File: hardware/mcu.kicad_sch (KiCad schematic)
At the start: 20 parts, among them J301 TagConnect, J302 USER CONN., U301 STM32G431, U302 SN65HVD230, Y301 12MHz

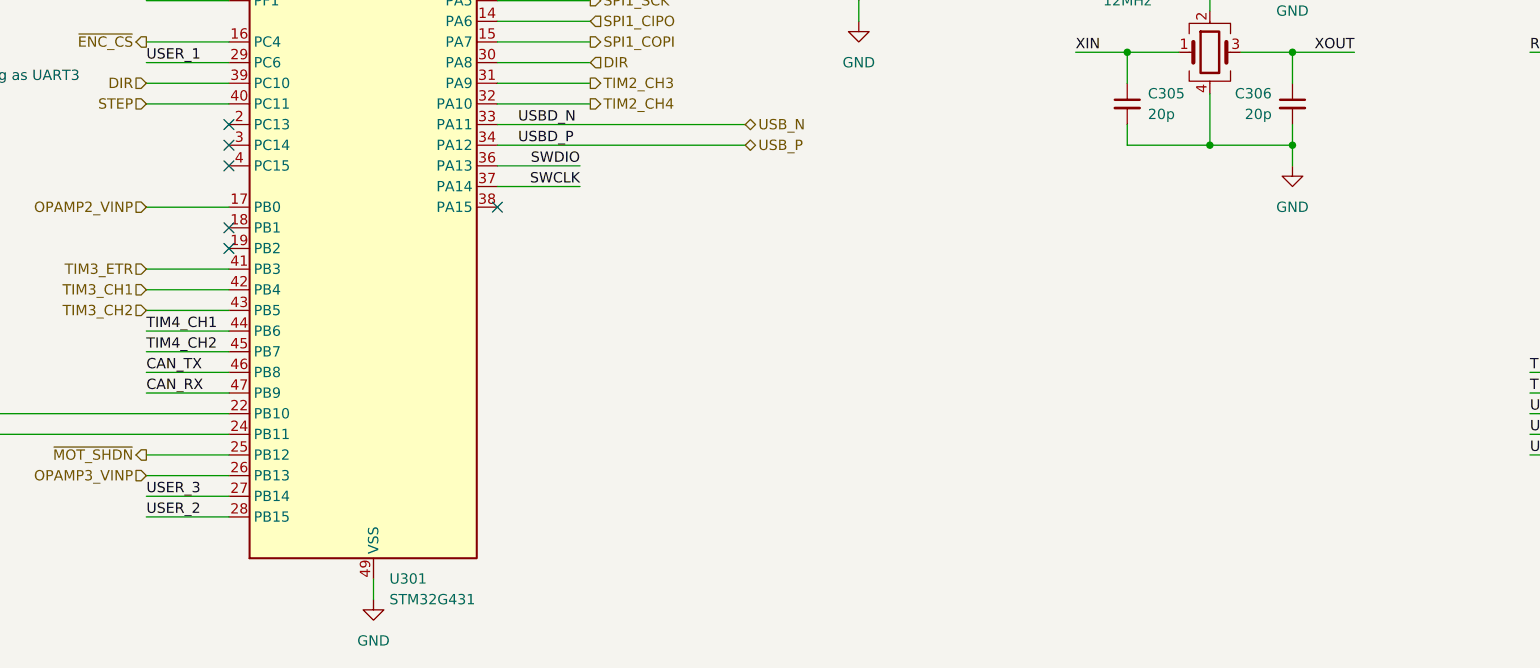
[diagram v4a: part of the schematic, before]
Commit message: add user button
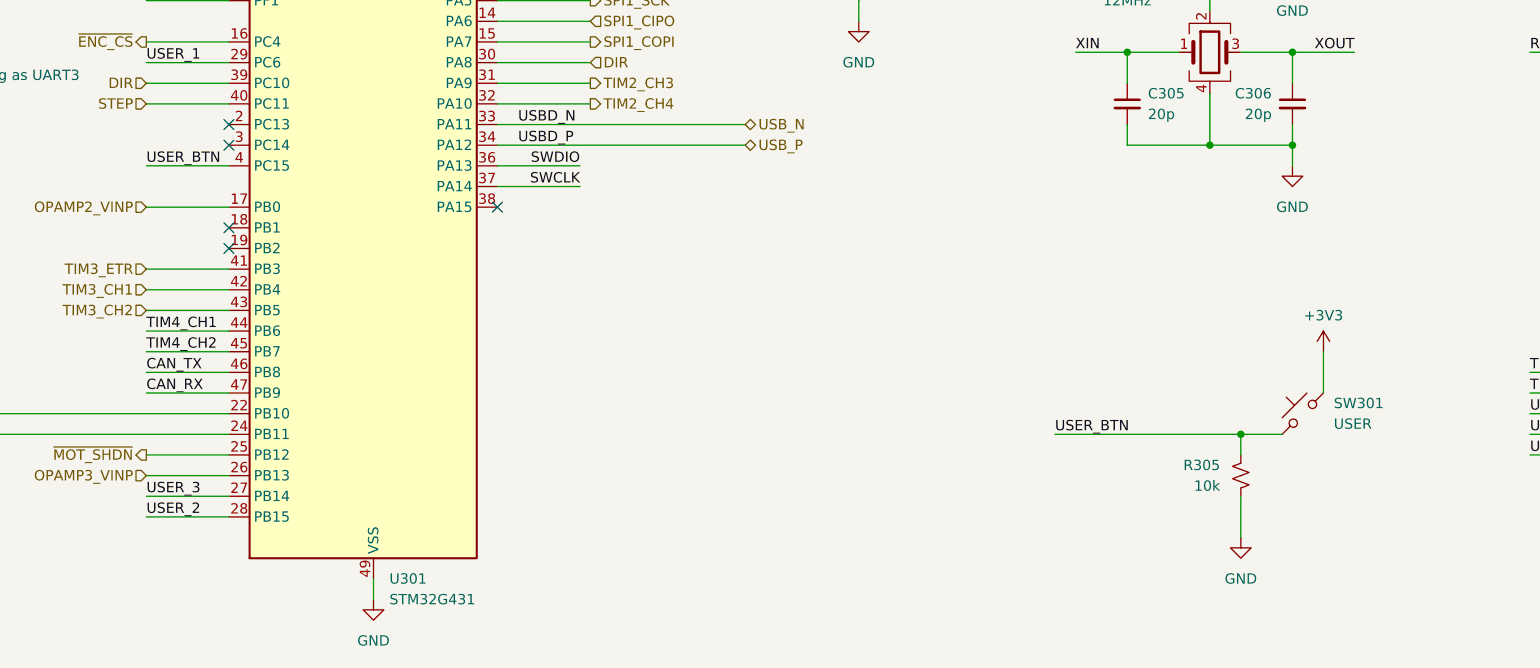
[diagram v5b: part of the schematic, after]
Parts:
- added R305: 10k, Resistor_SMD:R_0402_1005Metric, symbol Device:R_Small_US
- added SW301: USER, Button_Switch_SMD:SW_SPST_B3U-3000P, symbol Switch:SW_Push_45deg
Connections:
- net +3V3: now also SW301.2
- net GND: now also R305.2
- net USER_BTN: now reaches U301.4 (PC15)
- net USER_BTN: now also R305.1, SW301.1
- no-connect marks 10 -> 9
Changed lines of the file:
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@@
   (junction (at 186.69 90.17) (diameter 0) (color 0 0 0 0)
+  )
+  (junction (at 200.66 137.16) (diameter 0) (color 0 0 0 0)
   )
   (junction (at 123.19 52.07) (diameter 0) (color 0 0 0 0)
@@
   (no_connect (at 88.9 66.04))
   (no_connect (at 76.2 99.06))
-  (no_connect (at 76.2 104.14))
   (no_connect (at 76.2 111.76))
   (no_connect (at 76.2 114.3))
@@
     (stroke (width 0) (type default))
   )
+  (wire (pts (xy 200.66 137.16) (xy 205.74 137.16))
+    (stroke (width 0) (type default))
+  )
   (wire (pts (xy 232.41 48.26) (xy 243.84 48.26))
     (stroke (width 0) (type default))
@@
     (stroke (width 0) (type default))
   )
+  (wire (pts (xy 177.8 137.16) (xy 200.66 137.16))
+    (stroke (width 0) (type default))
+  )
   (wire (pts (xy 153.67 83.82) (xy 153.67 86.36))
     (stroke (width 0) (type default))
@@
     (stroke (width 0) (type default))
   )
+  (wire (pts (xy 210.82 127) (xy 210.82 132.08))
+    (stroke (width 0) (type default))
+  )
   (wire (pts (xy 123.19 58.42) (xy 123.19 59.69))
     (stroke (width 0) (type default))
@@
     (stroke (width 0) (type default))
   )
+  (wire (pts (xy 200.66 139.7) (xy 200.66 137.16))
+    (stroke (width 0) (type default))
+  )
   (wire (pts (xy 66.04 144.78) (xy 76.2 144.78))
     (stroke (width 0) (type default))
@@
     (stroke (width 0) (type default))
   )
+  (wire (pts (xy 66.04 104.14) (xy 76.2 104.14))
+    (stroke (width 0) (type default))
+  )
   (wire (pts (xy 133.35 52.07) (xy 133.35 53.34))
     (stroke (width 0) (type default))
@@
   )
   (wire (pts (xy 54.61 78.74) (xy 44.45 78.74))
+    (stroke (width 0) (type default))
+  )
+  (wire (pts (xy 200.66 144.78) (xy 200.66 149.86))
     (stroke (width 0) (type default))
   )
@@
     (effects (font (size 1.27 1.27)) (justify left bottom))
   )
+  (label "USER_BTN" (at 66.04 104.14 0) (fields_autoplaced)
+    (effects (font (size 1.27 1.27)) (justify left bottom))
+  )
   (label "USBD_N" (at 111.76 99.06 0) (fields_autoplaced)
     (effects (font (size 1.27 1.27)) (justify left bottom))
@@
   )
   (label "TIM4_CH1" (at 66.04 124.46 0) (fields_autoplaced)
+    (effects (font (size 1.27 1.27)) (justify left bottom))
+  )
+  (label "USER_BTN" (at 177.8 137.16 0) (fields_autoplaced)
     (effects (font (size 1.27 1.27)) (justify left bottom))
   )
@@
     )
   )
+  (symbol (lib_id "power:GND") (at 200.66 149.86 0) (unit 1)
+    (in_bom yes) (on_board yes) (dnp no) (fields_autoplaced)
+    (property "Reference" "#PWR0318" (at 200.66 156.21 0)
+      (effects (font (size 1.27 1.27)) hide)
+    )
+    (property "Value" "GND" (at 200.66 154.94 0)
+      (effects (font (size 1.27 1.27)))
+    )
+    (property "Footprint" "" (at 200.66 149.86 0)
+      (effects (font (size 1.27 1.27)) hide)
+    )
+    (property "Datasheet" "" (at 200.66 149.86 0)
+      (effects (font (size 1.27 1.27)) hide)
+    )
+    (pin "1")
+    (instances
+      (project "lemon-pepper"
+        (path "/0306e2fa-4433-4288-91d9-65a3484207ad/7f2d245a-6dca-4eb9-9839-7fdf255edd98"
+          (reference "#PWR0318") (unit 1)
+        )
+      )
+      (project "stm32g431-mt6701-stspin233"
+        (path "/bcb2c98d-7159-437a-9ffb-b81c5fcc4307"
+          (reference "#PWR0106") (unit 1)
+        )
+        (path "/bcb2c98d-7159-437a-9ffb-b81c5fcc4307/ed84ebbf-b2e5-4959-b495-bf58cd9b4c8c"
+          (reference "#PWR0204") (unit 1)
+        )
+      )
+    )
+  )
+  (symbol (lib_id "power:+3V3") (at 210.82 127 0) (unit 1)
+    (in_bom yes) (on_board yes) (dnp no) (fields_autoplaced)
+    (property "Reference" "#PWR0317" (at 210.82 130.81 0)
+      (effects (font (size 1.27 1.27)) hide)
+    )
+    (property "Value" "+3V3" (at 210.82 122.555 0)
+      (effects (font (size 1.27 1.27)))
+    )
+    (property "Footprint" "" (at 210.82 127 0)
+      (effects (font (size 1.27 1.27)) hide)
+    )
+    (property "Datasheet" "" (at 210.82 127 0)
+      (effects (font (size 1.27 1.27)) hide)
+    )
+    (pin "1")
+    (instances
+      (project "lemon-pepper"
+        (path "/0306e2fa-4433-4288-91d9-65a3484207ad/7f2d245a-6dca-4eb9-9839-7fdf255edd98"
+          (reference "#PWR0317") (unit 1)
+        )
+      )
+      (project "stm32g431-mt6701-stspin233"
+        (path "/bcb2c98d-7159-437a-9ffb-b81c5fcc4307"
+          (reference "#PWR0123") (unit 1)
+        )
+        (path "/bcb2c98d-7159-437a-9ffb-b81c5fcc4307/ed84ebbf-b2e5-4959-b495-bf58cd9b4c8c"
+          (reference "#PWR0210") (unit 1)
+        )
+      )
+    )
+  )
   (symbol (lib_id "Device:LED") (at 38.1 151.13 90) (unit 1)
     (in_bom yes) (on_board yes) (dnp no) (fields_autoplaced)
@@
         (path "/bcb2c98d-7159-437a-9ffb-b81c5fcc4307/ed84ebbf-b2e5-4959-b495-bf58cd9b4c8c"
           (reference "#PWR0210") (unit 1)
+        )
+      )
+    )
+  )
+  (symbol (lib_id "Switch:SW_Push_45deg") (at 208.28 134.62 90) (unit 1)
+    (in_bom yes) (on_board yes) (dnp no) (fields_autoplaced)
+    (property "Reference" "SW301" (at 212.09 133.35 90)
+      (effects (font (size 1.27 1.27)) (justify right))
+    )
+    (property "Value" "USER" (at 212.09 135.89 90)
+      (effects (font (size 1.27 1.27)) (justify right))
+    )
+    (property "Footprint" "Button_Switch_SMD:SW_SPST_B3U-3000P" (at 208.28 134.62 0)
+      (effects (font (size 1.27 1.27)) hide)
+    )
+    (property "Datasheet" "~" (at 208.28 134.62 0)
+      (effects (font (size 1.27 1.27)) hide)
+    )
+    (pin "1")
+    (pin "2")
+    (instances
+      (project "lemon-pepper"
+        (path "/0306e2fa-4433-4288-91d9-65a3484207ad/7f2d245a-6dca-4eb9-9839-7fdf255edd98"
+          (reference "SW301") (unit 1)
         )
       )
@@
         )
       )
+    )
+  )
+  (symbol (lib_id "Device:R_Small_US") (at 200.66 142.24 0) (mirror y) (unit 1)
+    (in_bom yes) (on_board yes) (dnp no)
+    (property "Reference" "R305" (at 198.12 140.97 0)
+      (effects (font (size 1.27 1.27)) (justify left))
+    )
+    (property "Value" "10k" (at 198.12 143.51 0)
+      (effects (font (size 1.27 1.27)) (justify left))
+    )
+    (property "Footprint" "Resistor_SMD:R_0402_1005Metric" (at 200.66 142.24 0)
+      (effects (font (size 1.27 1.27)) hide)
+    )
+    (property "Datasheet" "~" (at 200.66 142.24 0)
+      (effects (font (size 1.27 1.27)) hide)
+    )
+    (property "LCSC Part" "C25744" (at 200.66 142.24 0)
+      (effects (font (size 1.27 1.27)) hide)
+    )
+    (pin "1")
+    (pin "2")
+    (instances
+      (project "lemon-pepper"
+        (path "/0306e2fa-4433-4288-91d9-65a3484207ad/7f2d245a-6dca-4eb9-9839-7fdf255edd98"
+          (reference "R305") (unit 1)
+        )
+      )
+      (project "stm32g431-mt6701-stspin233"
+        (path "/bcb2c98d-7159-437a-9ffb-b81c5fcc4307"
+          (reference "R?") (unit 1)
+        )
+        (path "/bcb2c98d-7159-437a-9ffb-b81c5fcc4307/ed84ebbf-b2e5-4959-b495-bf58cd9b4c8c"
+          (reference "R203") (unit 1)
+        )
+      )

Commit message: finalize v3 files
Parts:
- SW301: LCSC Part (none) -> C963349
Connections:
- net LED_GOOD: now reaches R301.1, U301.22 (PB10)
- net LED_FAULT: now reaches R302.1, U301.24 (PB11)
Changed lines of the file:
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@@
+    (effects (font (size 1.27 1.27)) (justify left bottom))
+  )
+  (label "LED_GOOD" (at 66.04 134.62 0) (fields_autoplaced)
     (effects (font (size 1.27 1.27)) (justify left bottom))
   )
@@
     (effects (font (size 1.27 1.27)) (justify left bottom))
   )
+  (label "LED_FAULT" (at 66.04 137.16 0) (fields_autoplaced)
+    (effects (font (size 1.27 1.27)) (justify left bottom))
+  )
   (label "USER_1" (at 66.04 91.44 0) (fields_autoplaced)
     (effects (font (size 1.27 1.27)) (justify left bottom))
@@
       (effects (font (size 1.27 1.27)) hide)
     )
+    (property "LCSC Part" "C963349" (at 208.28 134.62 0)
+      (effects (font (size 1.27 1.27)) hide)
+    )

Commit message: rev3 documentation
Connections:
- net OPAMP2_VINP: no longer names the net of U301.17 (PB0)
- no-connect marks 9 -> 10
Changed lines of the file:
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@@
   (no_connect (at 109.22 76.2))
   (no_connect (at 76.2 101.6))
+  (no_connect (at 76.2 109.22))
   (no_connect (at 189.23 48.26))
   (no_connect (at 88.9 66.04))
@@
     (stroke (width 0) (type default))
   )
-  (wire (pts (xy 66.04 109.22) (xy 76.2 109.22))
-    (stroke (width 0) (type default))
-  )
   (wire (pts (xy 54.61 78.74) (xy 44.45 78.74))
     (stroke (width 0) (type default))
@@
     (effects (font (size 1.27 1.27)) (justify right))
   )
-  (hierarchical_label "OPAMP2_VINP" (shape input) (at 66.04 109.22 180) (fields_autoplaced)
-    (effects (font (size 1.27 1.27)) (justify right))
-  )

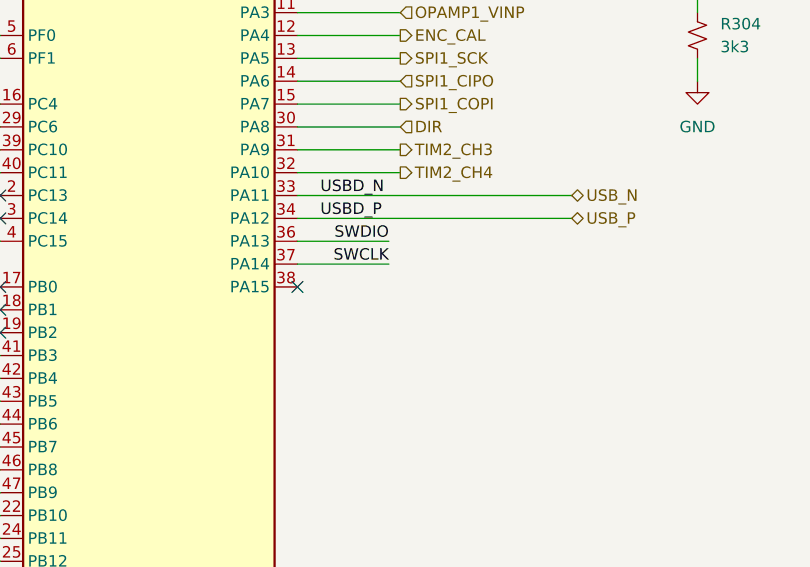
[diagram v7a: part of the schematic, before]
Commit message: change inductor footprint, add I2C1 SCL on user 3
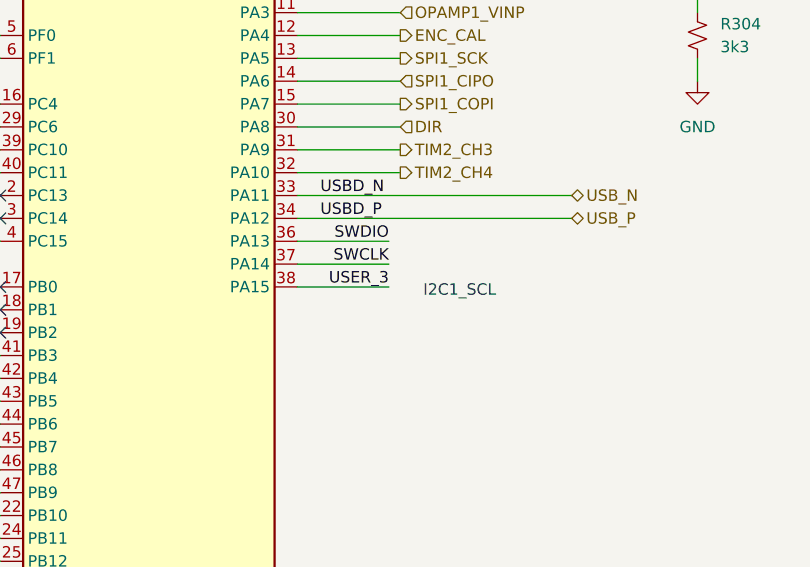
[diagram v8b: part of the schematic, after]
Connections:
- net USER_3: now also U301.38 (PA15)
- no-connect marks 10 -> 9
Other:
- note added: "I2C1_SCL"
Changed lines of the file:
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@@
   )
   (no_connect (at 243.84 50.8))
-  (no_connect (at 109.22 109.22))
   (no_connect (at 109.22 76.2))
   (no_connect (at 76.2 101.6))
@@
     (stroke (width 0) (type default))
   )
+  (wire (pts (xy 109.22 109.22) (xy 119.38 109.22))
+    (stroke (width 0) (type default))
+  )
   (wire (pts (xy 143.51 52.07) (xy 143.51 53.34))
     (stroke (width 0) (type default))
@@
   (wire (pts (xy 199.39 57.15) (xy 199.39 58.42))
     (stroke (width 0) (type default))
+  )
+  (text "I2C1_SCL" (at 123.19 110.49 0)
+    (effects (font (size 1.27 1.27)) (justify left bottom))
   )
   (text "really acting as UART3" (at 38.1 93.98 0)
@@
     (effects (font (size 1.27 1.27)) (justify left bottom))
   )
+  (label "USER_3" (at 119.38 109.22 180) (fields_autoplaced)
+    (effects (font (size 1.27 1.27)) (justify right bottom))
+  )
   (label "CAN_RX" (at 175.26 45.72 0) (fields_autoplaced)
